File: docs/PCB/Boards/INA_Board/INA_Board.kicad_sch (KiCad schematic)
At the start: 24 parts, among them J1 COM, J2 INA, Q1 AO3407A, SW1 SW_DIP_x02, U1 INA226AIDGST, U2 SIP32431DR3-T1GE3

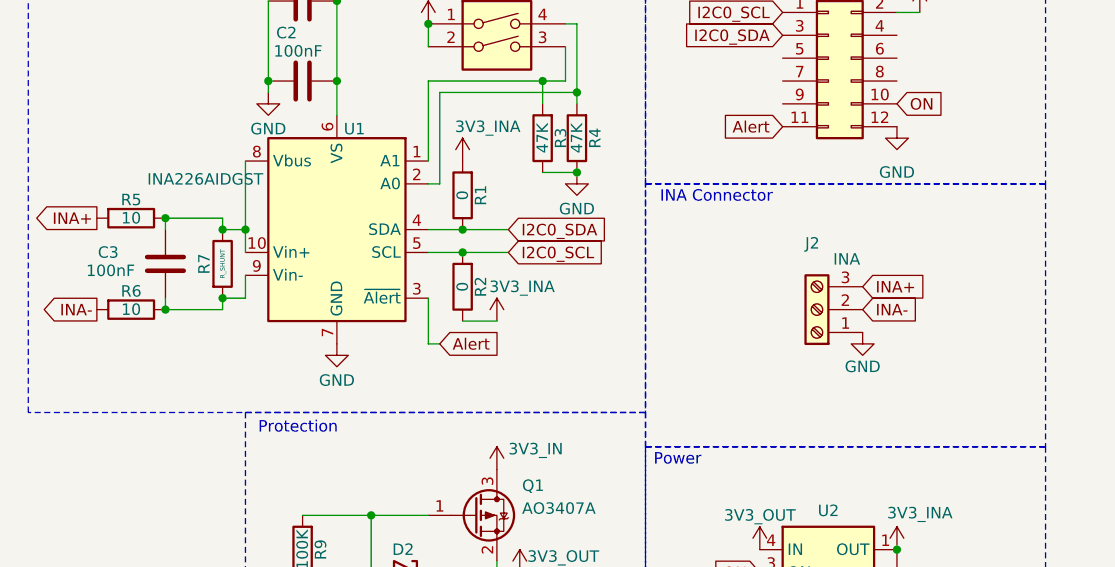
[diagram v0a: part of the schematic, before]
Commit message: Test program added, can protocol added.
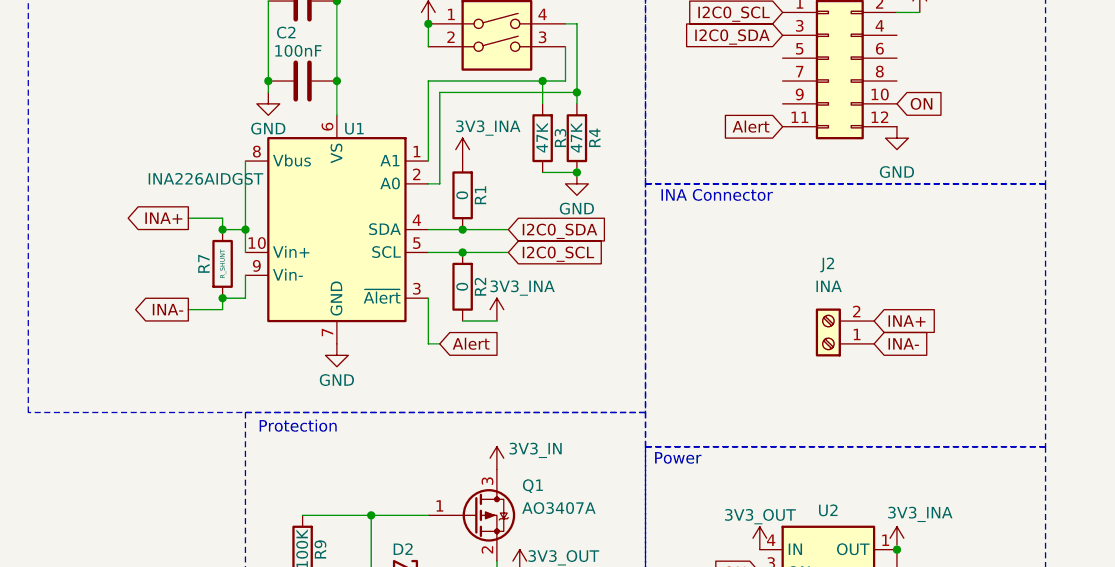
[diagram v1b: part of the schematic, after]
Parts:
- removed C3: 100nF, Capacitor_SMD:C_0805_2012Metric, symbol Device:C
- removed J2: INA, TerminalBlock_Phoenix:TerminalBlock_Phoenix_MKDS-1,5-3_1x03_P5.00mm_Horizontal, symbol Connector:Screw_Terminal_01x03
- removed R5, R6: 10, Resistor_SMD:R_0805_2012Metric, symbol Device:R
- added J2: INA, TerminalBlock_Phoenix:TerminalBlock_Phoenix_MKDS-1,5-2_1x02_P5.00mm_Horizontal, symbol Connector:Screw_Terminal_01x02
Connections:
- net INA+: now also R7.1, U1.10 (Vin+), U1.8 (Vbus), J2.2 (Pin_2)
- net INA-: now also R7.2, U1.9 (Vin-), J2.1 (Pin_1)

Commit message: Boards modified.
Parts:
- added C3, C4: 100nF, Capacitor_SMD:C_0805_2012Metric, symbol Device:C
- added R10, R5, R6: 10R, Resistor_SMD:R_0805_2012Metric, symbol Device:R
- R8: value 1K -> 4k7R
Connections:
- net GND: now also C4.1
- net INA+: now also R5.1; no longer U1.10 (Vin+), U1.8 (Vbus)
- net INA-: now also R6.1; no longer U1.9 (Vin-)
- new net: C4.2, R10.2, U1.8 (Vbus)
- new net: C3.2, R10.1, R5.2, U1.10 (Vin+)
- new net: C3.1, R6.2, U1.9 (Vin-)
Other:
- moved on the sheet: R7
